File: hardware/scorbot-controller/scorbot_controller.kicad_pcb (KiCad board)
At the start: 2 copper layers, 185 x 128 mm, 98 parts, among them J1 12V in (CUI PJ-102AH, 2.1 mm), J2 12V in (alt), J3 E-STOP (NC, in VM line), J4 DD-50 female R/A (robot cable), J5 I2C expansion, J6 Spare TCA9555 I/O, J7 FUSE (wire inline 5A fuse acr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, U1 DROK mini buck, set to 5V, U10 Pololu #4035 DRV8874 (M1), U11 Pololu #4035 DRV8874 (M2), U12 Pololu #4035 DRV8874 (M3), U13 Pololu #4035 DRV8874 (M4), U14 Pololu #4035 DRV8874 (M5), U15 Pololu #4035 DRV8874 (M6), U2 ESP32-DevKitC (WROOM-32D or -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, U5 TCA9555PWR (0x20), U6 ADS1115 module (0x48), U7 ADS1115 module (0x49)

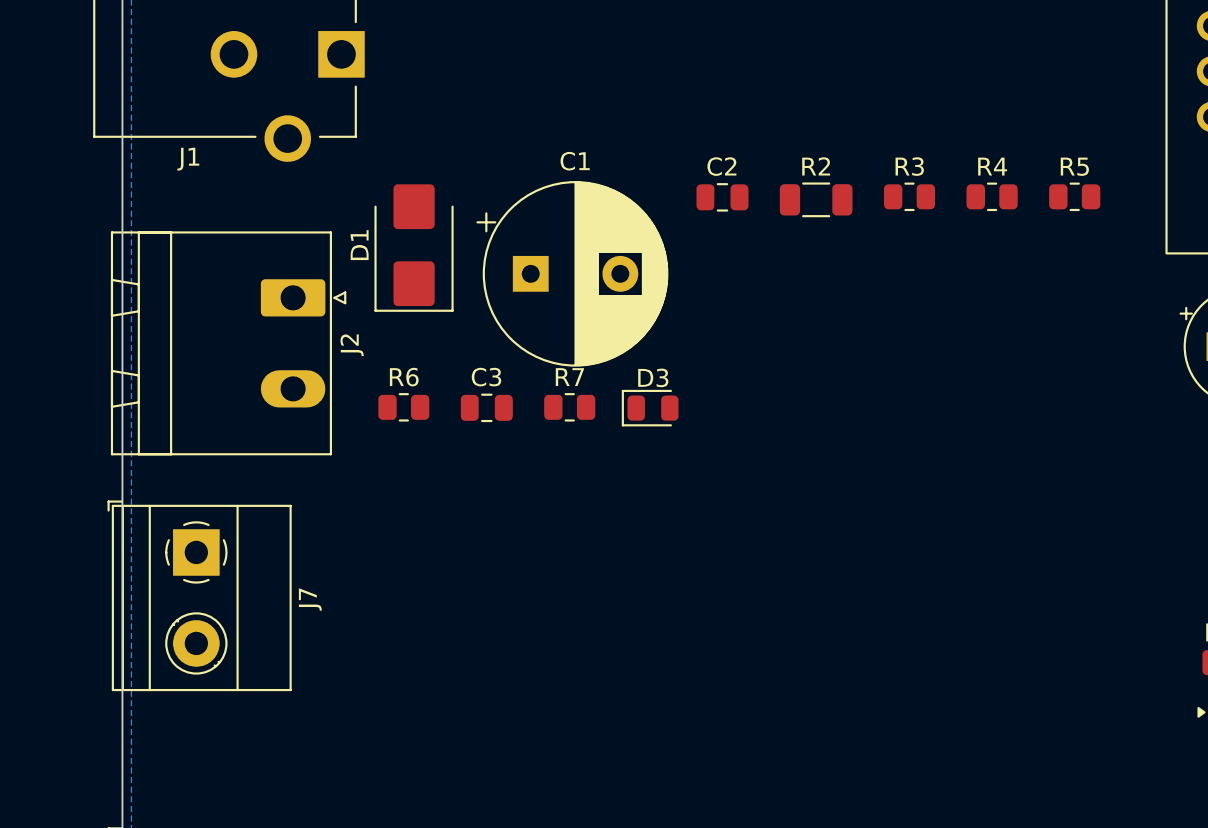
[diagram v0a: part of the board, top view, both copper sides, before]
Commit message: Board: screw-terminal power input beside the barrel jack, optional on-board blade fuse holder
- J2 is now a plain 5.08 mm screw terminal (alternative to barrel jack J1)
- F1 Keystone 3568 mini blade holder in parallel with the J7 fuse terminal; fit one
- Net classes for Power/Motor/Supply; gen_route.py autoroutes with Freerouting
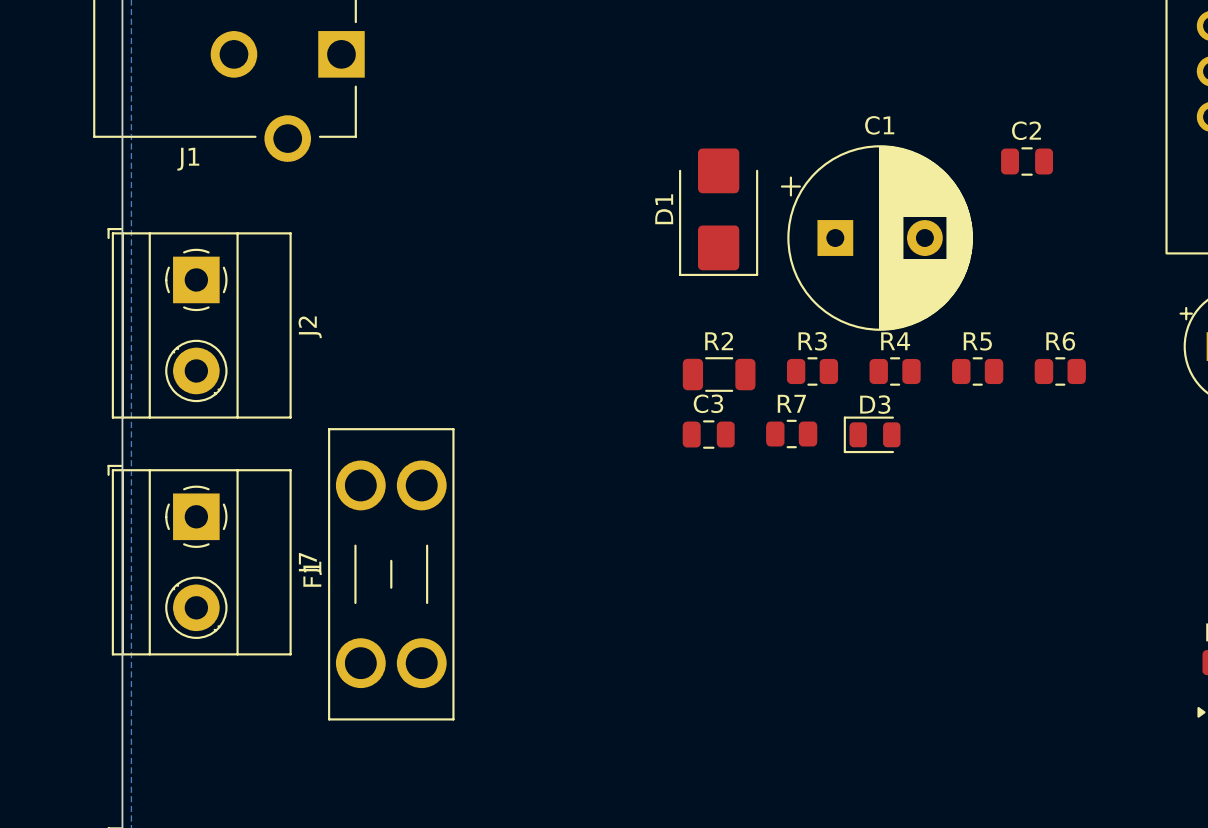
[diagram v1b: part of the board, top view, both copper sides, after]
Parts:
- added F1: 5A mini blade (Keystone 3568 holder), Fuse:Fuseholder_Blade_Mini_Keystone_3568, F.Cu at (43.3, 79.0)
- J2: value 12V in (alt) -> 12V in (screw terminal, +/-); footprint Connector_Phoenix_MSTB:PhoenixContact_MSTBA_2,5_2-G-5,08_1x02_P5.08mm_Horizontal -> TerminalBlock_Phoenix:TerminalBlock_Phoenix_MKDS-1,5-2-5.08_1x02_P5.08mm_Horizontal
- J7: value FUSE (wire inline 5A fuse across) -> FUSE alt: wire inline 5A fuse (fit F1 OR J7)
- moved R6 36.7 mm to (82.3, 62.7)
- moved C1 17.1 mm to (69.8, 55.3)
- moved D1 17.1 mm to (63.3, 53.7)
- moved C2 17.1 mm to (80.5, 51.0)
- moved R7 12.5 mm to (67.4, 66.2)
- moved C3 12.5 mm to (62.7, 66.2)
- moved D3 12.5 mm to (72.0, 66.3)
- moved R3 11.2 mm to (68.5, 62.7)
- moved R4 11.2 mm to (73.1, 62.7)
- moved R5 11.2 mm to (77.7, 62.7)
- moved R2 11.2 mm to (63.3, 62.9)
- moved J2 5.49 mm to (34.1, 57.6)
- moved J7 1.99 mm to (34.1, 70.8)

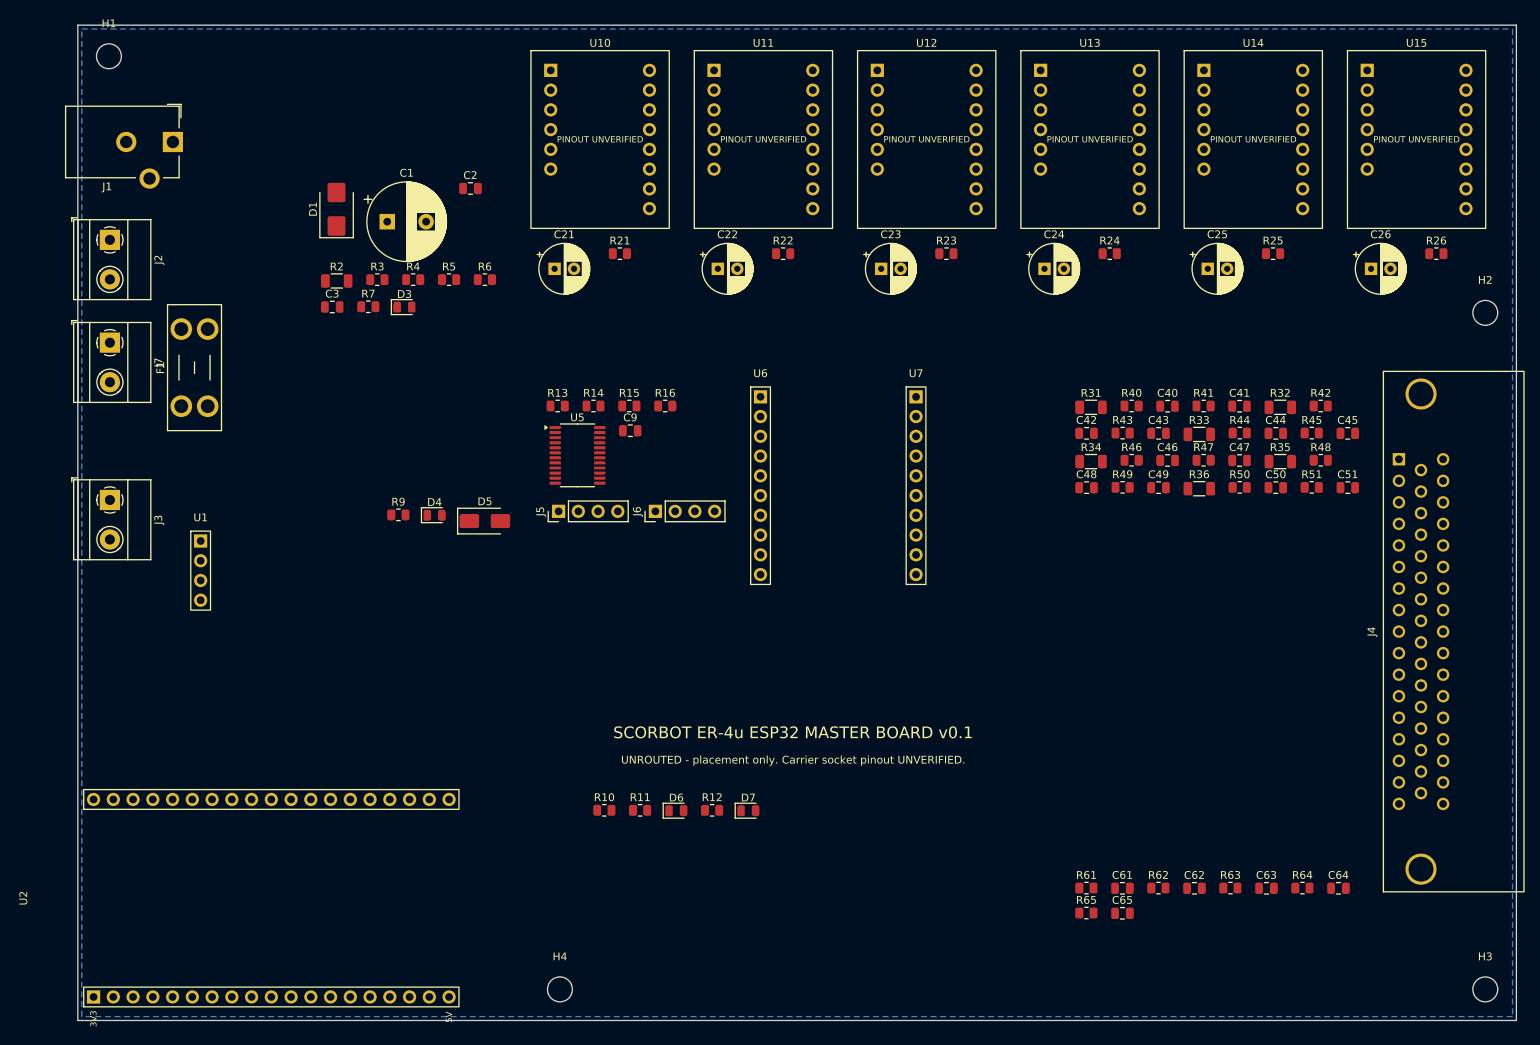
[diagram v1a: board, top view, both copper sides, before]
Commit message: Autoroute the master board with Freerouting
- gen_route.py: DSN export with per-class widths (Power 1.5 mm, Motor 0.8 mm,
  Supply 0.5 mm, GND 0.4 mm + pours), headless Freerouting, direct session
  import, GND pours on both layers with stitching vias, retry until complete
- DRC: 0 unconnected, 0 clearance errors
- Routed F/B previews in docs/
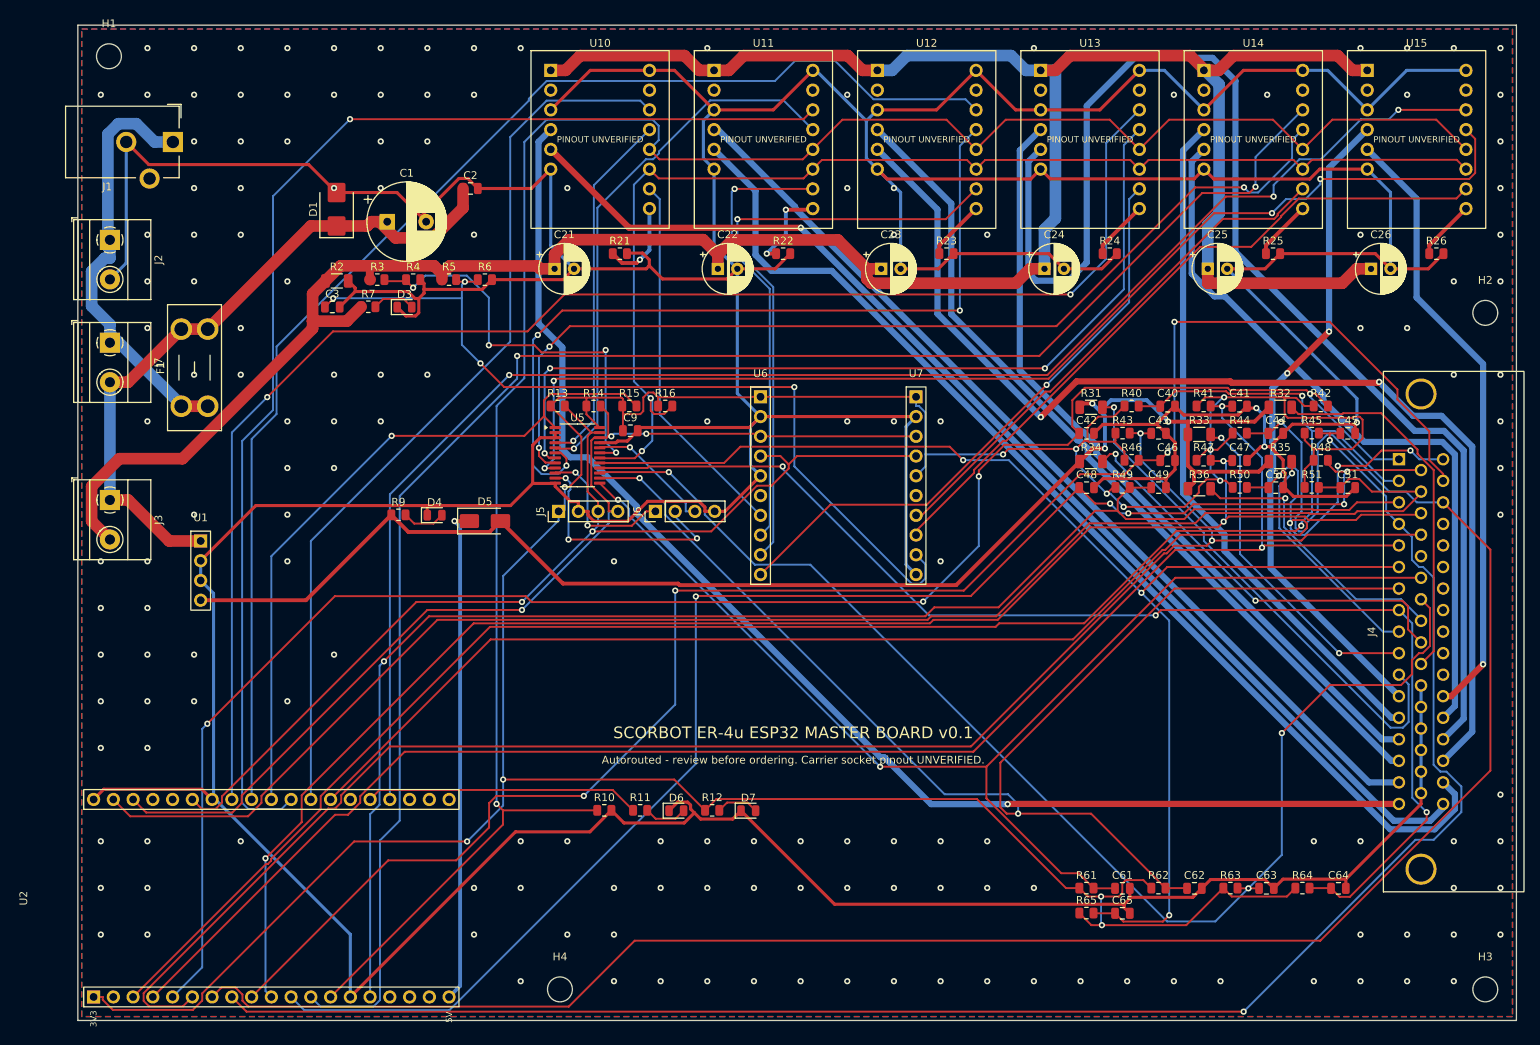
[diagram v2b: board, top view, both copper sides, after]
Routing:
- net GND: track 0.00 -> 1057.4 mm, vias 0 -> 164
- net +3V3: track 0.00 -> 452.1 mm, vias 0 -> 12
- net VM: track 0.00 -> 358.7 mm
- net NSLEEP: track 0.00 -> 274.1 mm, vias 0 -> 1
- net ENC3_P0: track 0.00 -> 269.5 mm, vias 0 -> 1
- net ENC1_P0: track 0.00 -> 230.2 mm, vias 0 -> 2
- net ENC3_P1: track 0.00 -> 228.8 mm, vias 0 -> 2
- net ENC2_P0: track 0.00 -> 225.2 mm, vias 0 -> 4
- net ENC4_P0: track 0.00 -> 220.9 mm, vias 0 -> 4
- net ENC2_P1: track 0.00 -> 217.7 mm, vias 0 -> 2
- net PWM5: track 0.00 -> 216.2 mm, vias 0 -> 2
- net ENC1_P1: track 0.00 -> 207.9 mm, vias 0 -> 2
- net ENC6_P1: track 0.00 -> 201.4 mm
- net PWM6: track 0.00 -> 199.0 mm, vias 0 -> 3
- net ENC4_P1: track 0.00 -> 198.4 mm, vias 0 -> 3
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- added copper zone on F.Cu, net GND
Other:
- board text added: "Autorouted - review before ordering. Carrier socket pinout UNVERIFIED."
- board text removed: "UNROUTED - placement only. Carrier socket pinout UNVERIFIED."

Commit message: v0.3: verified carrier pinout, on-board ADS1115s, wider power traces, SMD or THT TVS
- DRV8874 carrier socket from Pololu's labeled top view (2x7, 0.5in rows),
  VM/VIN orientation marks on the silkscreen
- ADS1115IDGSR x2 placed by JLC (0x48/0x49 by ADDR strap) replace the plug-in
  modules; 100nF decoupling each
- 1 oz copper: VIN/VM 2.5 mm with 1.6/0.8 mm vias, motor 1.2 mm with 1.2/0.6 mm vias
- D1 SMBJ18A (SMB) or D8 1.5KE18A (DO-201AD THT), hand-fitted, out of the JLC BOM
- JLC BOM grouped by LCSC part; README: how to check part numbers and orientation
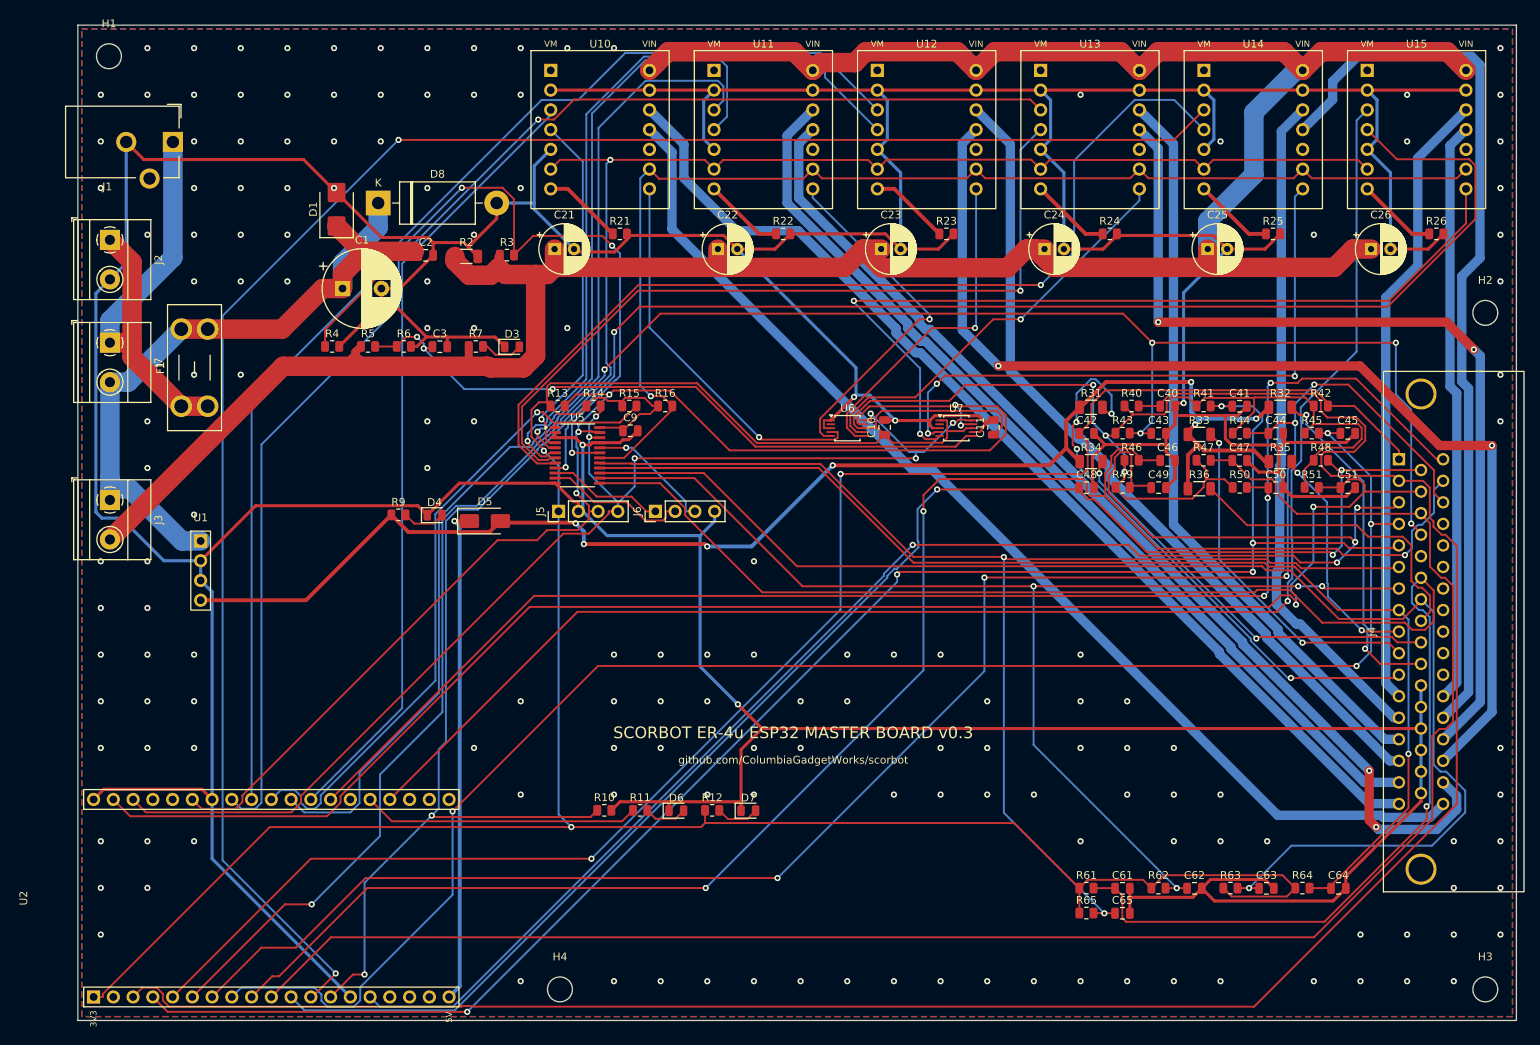
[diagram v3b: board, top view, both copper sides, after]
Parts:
- added C10: 100nF, Capacitor_SMD:C_0805_2012Metric, F.Cu at (133.8, 81.7)
- added C11: 100nF, Capacitor_SMD:C_0805_2012Metric, F.Cu at (147.8, 81.7)
- added D8: 1.5KE18A THT (fit D1 OR D8), Diode_THT:D_DO-201AD_P15.24mm_Horizontal, F.Cu at (68.6, 52.9)
- D1: value SMBJ18A (unidirectional) -> SMBJ18A (fit D1 OR D8)
- U6: value ADS1115 module (0x48) -> ADS1115IDGSR (0x48); footprint Scorbot:ADS1115_Module_Socket -> Package_SO:TSSOP-10_3x3mm_P0.5mm
- U7: value ADS1115 module (0x49) -> ADS1115IDGSR (0x49); footprint Scorbot:ADS1115_Module_Socket -> Package_SO:TSSOP-10_3x3mm_P0.5mm
- moved R3 17.0 mm to (85.2, 59.6)
- moved R2 17.0 mm to (80.0, 59.7)
- moved C3 14.7 mm to (76.6, 71.4)
- moved D3 14.7 mm to (85.8, 71.4)
- moved R7 14.7 mm to (81.2, 71.3)
- moved R4 13.5 mm to (62.7, 71.3)
- moved R5 13.5 mm to (67.3, 71.3)
- moved R6 13.5 mm to (71.9, 71.3)
- moved U6 11.9 mm to (129.0, 81.8)
- moved C2 10.3 mm to (74.7, 59.6)
- moved C1 10.3 mm to (64.0, 63.9)
- moved U7 6.56 mm to (143.0, 81.8)
- moved C21 2.54 mm to (91.3, 58.8)
- moved C22 2.54 mm to (112.3, 58.8)
- moved C23 2.54 mm to (133.3, 58.8)
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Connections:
- U10 pad 1: VM -> (no net)
- U10 pad 10: PH1 -> MOT1_A
- U10 pad 11: NSLEEP -> MOT1_B
- U10 pad 12: NFAULT -> (no net)
- U10 pad 13: CS1 -> NFAULT
- U10 pad 14: VREF1 -> CS1
- U10 pad 2: (no net) -> GND
- U10 pad 3: GND -> PWM1
- U10 pad 4: MOT1_A -> PH1
- U10 pad 5: MOT1_B -> GND
- U10 pad 6: GND -> NSLEEP
- U10 pad 7: GND -> VREF1
- U10 pad 8: (no net) -> VM
- U10 pad 9: PWM1 -> GND
- U11 pad 1: VM -> (no net)
- U11 pad 10: PH2 -> MOT2_A
- U11 pad 11: NSLEEP -> MOT2_B
- U11 pad 12: NFAULT -> (no net)
- U11 pad 13: CS2 -> NFAULT
- U11 pad 14: VREF2 -> CS2
- U11 pad 2: (no net) -> GND
- U11 pad 3: GND -> PWM2
- U11 pad 4: MOT2_A -> PH2
- U11 pad 5: MOT2_B -> GND
- U11 pad 6: GND -> NSLEEP
- U11 pad 7: GND -> VREF2
- U11 pad 8: (no net) -> VM
- U11 pad 9: PWM2 -> GND
- U12 pad 1: VM -> (no net)
- U12 pad 10: PH3 -> MOT3_A
- U12 pad 11: NSLEEP -> MOT3_B
- U12 pad 12: NFAULT -> (no net)
- U12 pad 13: CS3 -> NFAULT
- U12 pad 14: VREF3 -> CS3
- U12 pad 2: (no net) -> GND
- U12 pad 3: GND -> PWM3
- U12 pad 4: MOT3_A -> PH3
- U12 pad 5: MOT3_B -> GND
- U12 pad 6: GND -> NSLEEP
- U12 pad 7: GND -> VREF3
- U12 pad 8: (no net) -> VM
- U12 pad 9: PWM3 -> GND
- U13 pad 1: VM -> (no net)
- U13 pad 10: PH4 -> MOT4_A
- U13 pad 11: NSLEEP -> MOT4_B
- U13 pad 12: NFAULT -> (no net)
- U13 pad 13: CS4 -> NFAULT
- U13 pad 14: VREF4 -> CS4
- U13 pad 2: (no net) -> GND
- U13 pad 3: GND -> PWM4
- U13 pad 4: MOT4_A -> PH4
- U13 pad 5: MOT4_B -> GND
- U13 pad 6: GND -> NSLEEP
- U13 pad 7: GND -> VREF4
- U13 pad 8: (no net) -> VM
- U13 pad 9: PWM4 -> GND
- U14 pad 1: VM -> (no net)
- U14 pad 10: PH5 -> MOT5_A
- U14 pad 11: NSLEEP -> MOT5_B
- U14 pad 12: NFAULT -> (no net)
- U14 pad 13: CS5 -> NFAULT
- U14 pad 14: VREF5 -> CS5
- U14 pad 2: (no net) -> GND
- U14 pad 3: GND -> PWM5
- U14 pad 4: MOT5_A -> PH5
- U14 pad 5: MOT5_B -> GND
- U14 pad 6: GND -> NSLEEP
- U14 pad 7: GND -> VREF5
- U14 pad 8: (no net) -> VM
- U14 pad 9: PWM5 -> GND
- U15 pad 1: VM -> (no net)
- U15 pad 10: PH6 -> MOT6_A
- U15 pad 11: NSLEEP -> MOT6_B
- U15 pad 12: NFAULT -> (no net)
- U15 pad 13: CS6 -> NFAULT
- U15 pad 14: VREF6 -> CS6
- U15 pad 2: (no net) -> GND
- U15 pad 3: GND -> PWM6
- U15 pad 4: MOT6_A -> PH6
- U15 pad 5: MOT6_B -> GND
- U15 pad 6: GND -> NSLEEP
- U15 pad 7: GND -> VREF6
- U15 pad 8: (no net) -> VM
- U15 pad 9: PWM6 -> GND
- U6 pad 1: +3V3 -> GND
- U6 pad 10: CS4 -> SCL
- U6 pad 2: GND -> (no net)
- U6 pad 3: SCL -> GND
- U6 pad 4: SDA -> CS1
- U6 pad 5: GND -> CS2
- U6 pad 6: (no net) -> CS3
- U6 pad 7: CS1 -> CS4
- U6 pad 8: CS2 -> +3V3
- U6 pad 9: CS3 -> SDA
- U7 pad 10: GND -> SCL
- U7 pad 2: GND -> (no net)
- U7 pad 3: SCL -> GND
- U7 pad 4: SDA -> CS5
- U7 pad 5: +3V3 -> CS6
- U7 pad 6: (no net) -> VM_ADC
- U7 pad 7: CS5 -> GND
- U7 pad 8: CS6 -> +3V3
- U7 pad 9: VM_ADC -> SDA
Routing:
- net ENC1_P0: track 230.2 -> 282.8 mm, vias 2 -> 0
- net SW1: track 156.7 -> 207.3 mm, vias 2 -> 1
- net MOT4_B: track 168.6 -> 120.3 mm, vias 0 -> 2
- net ENC3_P0: track 269.5 -> 225.1 mm, vias 1 -> 5
- net SDA: track 136.9 -> 180.5 mm, vias 2 -> 5
- net +3V3: track 452.1 -> 491.5 mm, vias 12 -> 5
- net VM_SENSE: track 53.5 -> 90.0 mm
- net ENC2_P1: track 217.7 -> 253.8 mm, vias 2 -> 6
- net CS3: track 78.1 -> 43.5 mm
- net ENC4_P1: track 198.4 -> 232.3 mm, vias 3 -> 0
- net MOT1_A: track 170.1 -> 136.4 mm, vias 1 -> 0
- net PWM2: track 160.8 -> 133.7 mm, vias 1 -> 0
- net VM_ADC: track 111.5 -> 85.6 mm, vias 4 -> 3
- net CS4: track 77.0 -> 53.6 mm
- net ENC5_P1: track 190.3 -> 213.0 mm, vias 1 -> 4
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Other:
- board text added: "SCORBOT ER-4u ESP32 MASTER BOARD v0.3"
- board text added: "github.com/ColumbiaGadgetWorks/scorbot"
- board text removed: "Autorouted - review before ordering. Carrier socket pinout UNVERIFIED."
- board text removed: "SCORBOT ER-4u ESP32 MASTER BOARD v0.1"
